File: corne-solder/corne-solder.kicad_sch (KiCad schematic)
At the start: 47 parts, among them J1 Battery Connector, J2 nice!view, SW1 SW_Push, SW10 SW_Push, SW11 SW_Push, SW12 SW_Push, SW13 SW_Push, SW14 SW_Push, SW15 SW_Push, SW16 SW_Push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

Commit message: update
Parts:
- D1, D10, D11, D12, D13, D14, D15, D16, D17, D18, D19, D2, D20, D21, D3, D4, D5, D6, D7, D8, D9: footprint Project:D_SOD-123F-Reversible-Solder -> Project:Diode-Reversible
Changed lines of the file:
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@@
 			)
 		)
-		(property "Footprint" "Project:D_SOD-123F-Reversible-Solder"
+		(property "Footprint" "Project:Diode-Reversible"
 			(at 232.41 102.87 0)
 			(effects
@@
 			)
 		)
-		(property "Footprint" "Project:D_SOD-123F-Reversible-Solder"
+		(property "Footprint" "Project:Diode-Reversible"
 			(at 214.63 120.65 0)
 			(effects
@@
 			)
 		)
-		(property "Footprint" "Project:D_SOD-123F-Reversible-Solder"
+		(property "Footprint" "Project:Diode-Reversible"
 			(at 250.19 156.21 0)
 			(effects
@@
 			)
 		)
-		(property "Footprint" "Project:D_SOD-123F-Reversible-Solder"
+		(property "Footprint" "Project:Diode-Reversible"
 			(at 214.63 138.43 0)
 			(effects
@@
 			)
 		)
-		(property "Footprint" "Project:D_SOD-123F-Reversible-Solder"
+		(property "Footprint" "Project:Diode-Reversible"
 			(at 196.85 120.65 0)
 			(effects
@@
 			)
 		)
-		(property "Footprint" "Project:D_SOD-123F-Reversible-Solder"
+		(property "Footprint" "Project:Diode-Reversible"
 			(at 179.07 102.87 0)
 			(effects
@@
 			)
 		)
-		(property "Footprint" "Project:D_SOD-123F-Reversible-Solder"
+		(property "Footprint" "Project:Diode-Reversible"
 			(at 179.07 138.43 0)
 			(effects
@@
 			)
 		)
-		(property "Footprint" "Project:D_SOD-123F-Reversible-Solder"
+		(property "Footprint" "Project:Diode-Reversible"
 			(at 179.07 120.65 0)
 			(effects
@@
 			)
 		)
-		(property "Footprint" "Project:D_SOD-123F-Reversible-Solder"
+		(property "Footprint" "Project:Diode-Reversible"
 			(at 196.85 102.87 0)
 			(effects
@@
 			)
 		)
-		(property "Footprint" "Project:D_SOD-123F-Reversible-Solder"
+		(property "Footprint" "Project:Diode-Reversible"
 			(at 267.97 102.87 0)
 			(effects
@@
 			)
 		)
-		(property "Footprint" "Project:D_SOD-123F-Reversible-Solder"
+		(property "Footprint" "Project:Diode-Reversible"
 			(at 267.97 138.43 0)
 			(effects
@@
 			)
 		)
-		(property "Footprint" "Project:D_SOD-123F-Reversible-Solder"
+		(property "Footprint" "Project:Diode-Reversible"
 			(at 214.63 102.87 0)
 			(effects
@@
 			)
 		)
-		(property "Footprint" "Project:D_SOD-123F-Reversible-Solder"
+		(property "Footprint" "Project:Diode-Reversible"
 			(at 267.97 156.21 0)
 			(effects
@@
 			)
 		)
-		(property "Footprint" "Project:D_SOD-123F-Reversible-Solder"
+		(property "Footprint" "Project:Diode-Reversible"
 			(at 232.41 120.65 0)
 			(effects
@@
 			)
 		)
-		(property "Footprint" "Project:D_SOD-123F-Reversible-Solder"
+		(property "Footprint" "Project:Diode-Reversible"
 			(at 250.19 138.43 0)
 			(effects
@@
 			)
 		)
-		(property "Footprint" "Project:D_SOD-123F-Reversible-Solder"
+		(property "Footprint" "Project:Diode-Reversible"
 			(at 232.41 156.21 0)
 			(effects
@@
 			)
 		)
-		(property "Footprint" "Project:D_SOD-123F-Reversible-Solder"
+		(property "Footprint" "Project:Diode-Reversible"
 			(at 267.97 120.65 0)
 			(effects
@@
 			)
 		)
-		(property "Footprint" "Project:D_SOD-123F-Reversible-Solder"
+		(property "Footprint" "Project:Diode-Reversible"
 			(at 196.85 138.43 0)
 			(effects
@@
 			)
 		)
-		(property "Footprint" "Project:D_SOD-123F-Reversible-Solder"
+		(property "Footprint" "Project:Diode-Reversible"
 			(at 250.19 102.87 0)
 			(effects
@@
 			)
 		)
-		(property "Footprint" "Project:D_SOD-123F-Reversible-Solder"
+		(property "Footprint" "Project:Diode-Reversible"
 			(at 250.19 120.65 0)
 			(effects
@@
 			)
 		)
-		(property "Footprint" "Project:D_SOD-123F-Reversible-Solder"
+		(property "Footprint" "Project:Diode-Reversible"
 			(at 232.41 138.43 0)
 			(effects

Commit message: wiring
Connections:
- net GND: now also J1.1 (Pin_1); no longer J1.2 (Pin_2)
- net at PSW1.2 (B): now also J1.2 (Pin_2); no longer J1.1 (Pin_1)
- no-connect marks 3 -> 6
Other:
- moved on the sheet: J1
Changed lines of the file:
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@@
 	)
 	(no_connect
+		(at 45.72 74.93)
+	)
+	(no_connect
 		(at 45.72 52.07)
 	)
 	(no_connect
+		(at 71.12 77.47)
+	)
+	(no_connect
 		(at 45.72 49.53)
 	)
@@
 		(at 48.26 101.6)
 	)
+	(no_connect
+		(at 71.12 74.93)
+	)
 	(wire
 		(pts
@@
 	(wire
 		(pts
+			(xy 66.04 104.14) (xy 58.42 104.14)
+		)
+		(stroke
+			(width 0)
+			(type default)
+		)
+	)
+	(wire
+		(pts
 			(xy 257.81 90.17) (xy 257.81 99.06)
 		)
@@
 	(wire
 		(pts
-			(xy 58.42 104.14) (xy 66.04 104.14)
-		)
-		(stroke
-			(width 0)
-			(type default)
-		)
-	)
-	(wire
-		(pts
 			(xy 168.91 116.84) (xy 168.91 134.62)
 		)
@@
 	(symbol
 		(lib_id "Connector_Generic:Conn_01x02")
-		(at 71.12 104.14 0)
+		(at 71.12 101.6 0)
 		(unit 1)
 		(exclude_from_sim no)
@@
 		(fields_autoplaced yes)
 		(property "Reference" "J1"
-			(at 73.66 104.1399 0)
+			(at 73.66 101.5999 0)
 			(effects
 				(font
@@
 		)
 		(property "Value" "Battery Connector"
-			(at 73.66 106.6799 0)
+			(at 73.66 104.1399 0)
 			(effects
 				(font
@@
 		)
 		(property "Footprint" "Connector_JST:JST_PH_S2B-PH-K_1x02_P2.00mm_Horizontal"
-			(at 71.12 104.14 0)
+			(at 71.12 101.6 0)
 			(effects
 				(font
@@
 		)
 		(property "Datasheet" "~"
-			(at 71.12 104.14 0)
+			(at 71.12 101.6 0)
 			(effects
 				(font
@@
 		)
 		(property "Description" "Generic connector, single row, 01x02, script generated (kicad-library-utils/schlib/autogen/connector/)"
-			(at 71.12 104.14 0)
+			(at 71.12 101.6 0)
 			(effects
 				(font
@@
 	)
 	(symbol
-		(lib_id "power:GND")
-		(at 66.04 106.68 270)
-		(unit 1)
-		(exclude_from_sim no)
-		(in_bom yes)
-		(on_board yes)
-		(dnp no)
-		(fields_autoplaced yes)
-		(property "Reference" "#PWR02"
-			(at 59.69 106.68 0)
-			(effects
-				(font
-					(size 1.27 1.27)
-				)
-				(hide yes)
-			)
-		)
-		(property "Value" "GND"
-			(at 62.23 106.6799 90)
-			(effects
-				(font
-					(size 1.27 1.27)
-				)
-				(justify right)
-			)
-		)
-		(property "Footprint" ""
-			(at 66.04 106.68 0)
-			(effects
-				(font
-					(size 1.27 1.27)
-				)
-				(hide yes)
-			)
-		)
-		(property "Datasheet" ""
-			(at 66.04 106.68 0)
-			(effects
-				(font
-					(size 1.27 1.27)
-				)
-				(hide yes)
-			)
-		)
-		(property "Description" "Power symbol creates a global label with name \"GND\" , ground"
-			(at 66.04 106.68 0)
-			(effects
-				(font
-					(size 1.27 1.27)
-				)
-				(hide yes)
-			)
-		)
-		(pin "1"
-		)
-		(instances
-			(project "corne-hotswap"
-				(path "/a84e1b1a-6de0-41da-b249-d0af4d1e6311"
-					(reference "#PWR02")
-					(unit 1)
-				)
-			)
-		)
-	)
-	(symbol
 		(lib_id "Device:D")
 		(at 196.85 120.65 90)
@@
 					(unit 1)
 				)
+			)
+		)
+	)
+	(symbol
+		(lib_id "power:GND")
+		(at 66.04 101.6 270)
+		(unit 1)
+		(exclude_from_sim no)
+		(in_bom yes)
+		(on_board yes)
+		(dnp no)
+		(fields_autoplaced yes)
+		(property "Reference" "#PWR02"
+			(at 59.69 101.6 0)
+			(effects
+				(font
+					(size 1.27 1.27)
+				)
+				(hide yes)
+			)
+		)
+		(property "Value" "GND"
+			(at 62.23 101.5999 90)
+			(effects
+				(font
+					(size 1.27 1.27)
+				)
+				(justify right)
+			)
+		)
+		(property "Footprint" ""
+			(at 66.04 101.6 0)
+			(effects
+				(font
+					(size 1.27 1.27)
+				)
+				(hide yes)
+			)
+		)
+		(property "Datasheet" ""
+			(at 66.04 101.6 0)
+			(effects
+				(font
+					(size 1.27 1.27)
+				)
+				(hide yes)
+			)
+		)
+		(property "Description" "Power symbol creates a global label with name \"GND\" , ground"
+			(at 66.04 101.6 0)
+			(effects
+				(font
+					(size 1.27 1.27)
+				)
+				(hide yes)
+			)
+		)
+		(pin "1"
+		)
+		(instances
+			(project "corne-solder"
+				(path "/a84e1b1a-6de0-41da-b249-d0af4d1e6311"
+					(reference "#PWR02")
+					(unit 1)
+				)

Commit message: More jump pads
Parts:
- J1: footprint Connector_JST:JST_PH_S2B-PH-K_1x02_P2.00mm_Horizontal -> Project:JST_PH_S2B-PH-K_1x02_P2.00mm_Horizontal
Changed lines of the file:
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@@
 			)
 		)
-		(property "Footprint" "Connector_JST:JST_PH_S2B-PH-K_1x02_P2.00mm_Horizontal"
+		(property "Footprint" "Project:JST_PH_S2B-PH-K_1x02_P2.00mm_Horizontal"
 			(at 71.12 101.6 0)
 			(effects

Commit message: add bridge for wired
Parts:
- added J3: USB_C_Receptacle_PowerOnly_6P, Project:USB_C_Receptacle_GCT_USB4125-xx-x_6P_TopMnt_Horizontal, symbol Connector:USB_C_Receptacle_PowerOnly_6P
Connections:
- net GND: now also J3.A12 (GND), J3.B12 (GND), J3.S1 (SHIELD)
- net VCC: now also J3.A9 (VBUS), J3.B9 (VBUS)
- net RX: now reaches U1.2 (D2-RX)
- net RX: now also J3.A5 (CC1), J3.B5 (CC2)
- no-connect marks 6 -> 5
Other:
- moved on the sheet: J1, J2, PSW1, RSW1

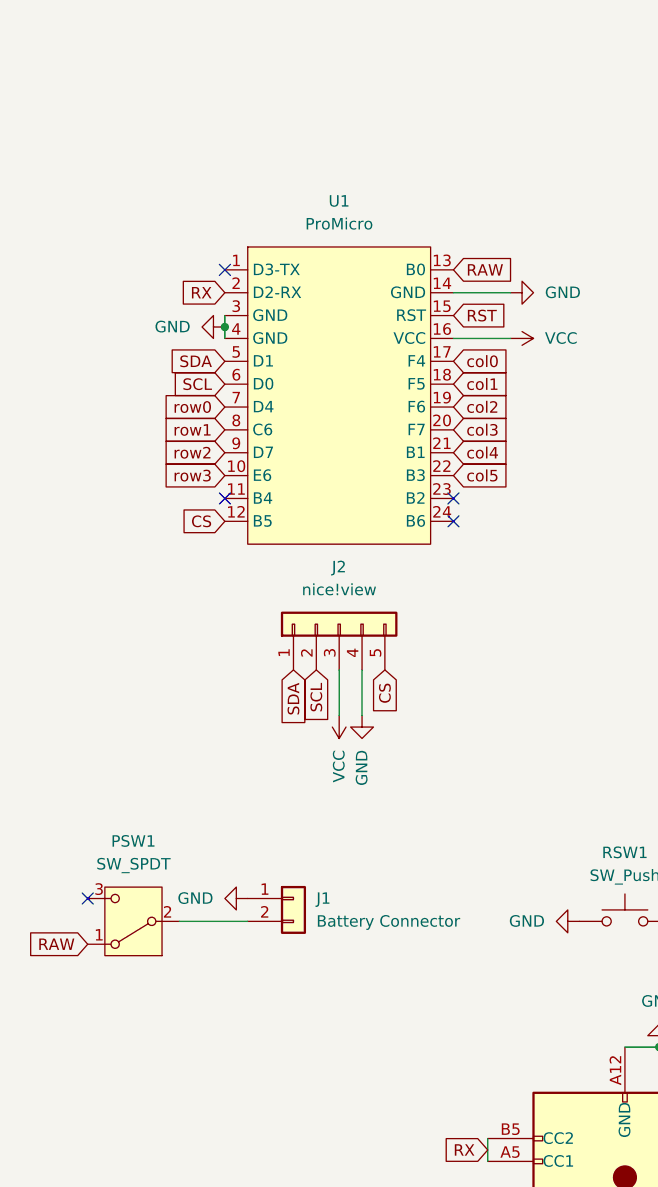
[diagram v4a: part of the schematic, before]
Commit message: add battery wire pads
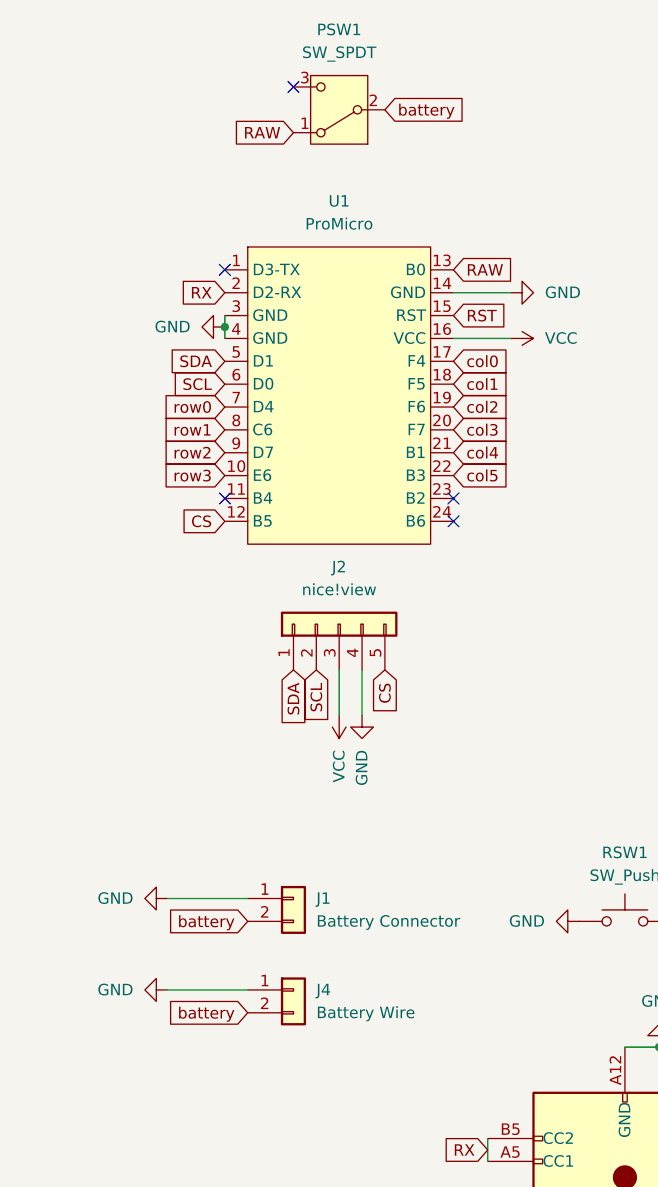
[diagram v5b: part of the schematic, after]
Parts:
- added J4: Battery Wire, Project:Battery Wire, symbol Connector_Generic:Conn_01x02
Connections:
- net GND: now also J4.1 (Pin_1)
- net battery: now reaches J1.2 (Pin_2), PSW1.2 (B)
- net battery: now also J4.2 (Pin_2)
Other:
- moved on the sheet: PSW1
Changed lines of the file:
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@@
 	)
 	(no_connect
-		(at 30.48 119.38)
+		(at 53.34 29.21)
 	)
 	(no_connect
@@
 	(wire
 		(pts
-			(xy 48.26 121.92) (xy 40.64 121.92)
-		)
-		(stroke
-			(width 0)
-			(type default)
-		)
-	)
-	(wire
-		(pts
 			(xy 257.81 90.17) (xy 257.81 99.06)
 		)
@@
 	(wire
 		(pts
+			(xy 39.37 119.38) (xy 48.26 119.38)
+		)
+		(stroke
+			(width 0)
+			(type default)
+		)
+	)
+	(wire
+		(pts
 			(xy 267.97 124.46) (xy 273.05 124.46)
 		)
@@
 	(wire
 		(pts
+			(xy 39.37 129.54) (xy 48.26 129.54)
+		)
+		(stroke
+			(width 0)
+			(type default)
+		)
+	)
+	(wire
+		(pts
 			(xy 179.07 124.46) (xy 196.85 124.46)
 		)
@@
 		)
 	)
+	(global_label "battery"
+		(shape input)
+		(at 63.5 31.75 0)
+		(fields_autoplaced yes)
+		(effects
+			(font
+				(size 1.27 1.27)
+			)
+			(justify left)
+		)
+		(property "Intersheetrefs" "${INTERSHEET_REFS}"
+			(at 73.077 31.75 0)
+			(effects
+				(font
+					(size 1.27 1.27)
+				)
+				(justify left)
+				(hide yes)
+			)
+		)
+	)
 	(global_label "col5"
 		(shape input)
@@
 	(global_label "RAW"
 		(shape input)
-		(at 30.48 124.46 180)
+		(at 53.34 34.29 180)
 		(fields_autoplaced yes)
 		(effects
@@
 		)
 		(property "Intersheetrefs" "${INTERSHEET_REFS}"
-			(at 23.6848 124.46 0)
+			(at 46.5448 34.29 0)
 			(effects
 				(font
@@
 		)
 	)
+	(global_label "battery"
+		(shape input)
+		(at 48.26 132.08 180)
+		(fields_autoplaced yes)
+		(effects
+			(font
+				(size 1.27 1.27)
+			)
+			(justify right)
+		)
+		(property "Intersheetrefs" "${INTERSHEET_REFS}"
+			(at 38.683 132.08 0)
+			(effects
+				(font
+					(size 1.27 1.27)
+				)
+				(justify right)
+				(hide yes)
+			)
+		)
+	)
 	(global_label "col5"
 		(shape input)
@@
 		)
 	)
+	(global_label "battery"
+		(shape input)
+		(at 48.26 121.92 180)
+		(fields_autoplaced yes)
+		(effects
+			(font
+				(size 1.27 1.27)
+			)
+			(justify right)
+		)
+		(property "Intersheetrefs" "${INTERSHEET_REFS}"
+			(at 38.683 121.92 0)
+			(effects
+				(font
+					(size 1.27 1.27)
+				)
+				(justify right)
+				(hide yes)
+			)
+		)
+	)
 	(symbol
 		(lib_id "power:VCC")
@@
 	)
 	(symbol
+		(lib_id "Connector_Generic:Conn_01x02")
+		(at 53.34 129.54 0)
+		(unit 1)
+		(exclude_from_sim no)
+		(in_bom yes)
+		(on_board yes)
+		(dnp no)
+		(fields_autoplaced yes)
+		(property "Reference" "J4"
+			(at 55.88 129.5399 0)
+			(effects
+				(font
+					(size 1.27 1.27)
+				)
+				(justify left)
+			)
+		)
+		(property "Value" "Battery Wire"
+			(at 55.88 132.0799 0)
+			(effects
+				(font
+					(size 1.27 1.27)
+				)
+				(justify left)
+			)
+		)
+		(property "Footprint" "Project:Battery Wire"
+			(at 53.34 129.54 0)
+			(effects
+				(font
+					(size 1.27 1.27)
+				)
+				(hide yes)
+			)
+		)
+		(property "Datasheet" "~"
+			(at 53.34 129.54 0)
+			(effects
+				(font
+					(size 1.27 1.27)
+				)
+				(hide yes)
+			)
+		)
+		(property "Description" "Generic connector, single row, 01x02, script generated (kicad-library-utils/schlib/autogen/connector/)"
+			(at 53.34 129.54 0)
+			(effects
+				(font
+					(size 1.27 1.27)
+				)
+				(hide yes)
+			)
+		)
+		(pin "2"
+		)
+		(pin "1"
+		)
+		(instances
+			(project "corne-solder"
+				(path "/a84e1b1a-6de0-41da-b249-d0af4d1e6311"
+					(reference "J4")
+					(unit 1)
+				)
+			)
+		)
+	)
+	(symbol
+		(lib_id "power:GND")
+		(at 39.37 129.54 270)
+		(unit 1)
+		(exclude_from_sim no)
+		(in_bom yes)
+		(on_board yes)
+		(dnp no)
+		(fields_autoplaced yes)
+		(property "Reference" "#PWR010"
+			(at 33.02 129.54 0)
+			(effects
+				(font
+					(size 1.27 1.27)
+				)
+				(hide yes)
+			)
+		)
+		(property "Value" "GND"
+			(at 35.56 129.5399 90)
+			(effects
+				(font
+					(size 1.27 1.27)
+				)
+				(justify right)
+			)
+		)
+		(property "Footprint" ""
+			(at 39.37 129.54 0)
+			(effects
+				(font
+					(size 1.27 1.27)
+				)
+				(hide yes)
+			)
+		)
+		(property "Datasheet" ""
+			(at 39.37 129.54 0)
+			(effects
+				(font
+					(size 1.27 1.27)
+				)
+				(hide yes)
+			)
+		)
+		(property "Description" "Power symbol creates a global label with name \"GND\" , ground"
+			(at 39.37 129.54 0)
+			(effects
+				(font
+					(size 1.27 1.27)
+				)
+				(hide yes)
+			)
+		)
+		(pin "1"
+		)
+		(instances
+			(project "corne-solder"
+				(path "/a84e1b1a-6de0-41da-b249-d0af4d1e6311"
+					(reference "#PWR010")
+					(unit 1)
+				)
+			)
+		)
+	)
+	(symbol
 		(lib_id "power:GND")
 		(at 60.96 99.06 0)
@@
 	(symbol
 		(lib_id "power:GND")
-		(at 48.26 119.38 270)
+		(at 39.37 119.38 270)
 		(unit 1)
 		(exclude_from_sim no)
@@
 		(fields_autoplaced yes)
 		(property "Reference" "#PWR02"
-			(at 41.91 119.38 0)
+			(at 33.02 119.38 0)
 			(effects
 				(font
@@
 		)
 		(property "Value" "GND"
-			(at 44.45 119.3799 90)
+			(at 35.56 119.3799 90)
 			(effects
 				(font
@@
 		)
 		(property "Footprint" ""
-			(at 48.26 119.38 0)
+			(at 39.37 119.38 0)
 			(effects
 				(font
@@
 		)
 		(property "Datasheet" ""
-			(at 48.26 119.38 0)
+			(at 39.37 119.38 0)
 			(effects
 				(font
@@
 		)
 		(property "Description" "Power symbol creates a global label with name \"GND\" , ground"
-			(at 48.26 119.38 0)
+			(at 39.37 119.38 0)
 			(effects
 				(font
@@
 	(symbol
 		(lib_id "Switch:SW_SPDT")
-		(at 35.56 121.92 180)
+		(at 58.42 31.75 180)
 		(unit 1)
 		(exclude_from_sim no)
@@
 		(fields_autoplaced yes)
 		(property "Reference" "PSW1"
-			(at 35.56 113.03 0)
+			(at 58.42 22.86 0)
 			(effects
 				(font
@@
 		)
 		(property "Value" "SW_SPDT"
-			(at 35.56 115.57 0)
+			(at 58.42 25.4 0)
 			(effects
 				(font
@@
 		)
 		(property "Footprint" "Project:SW_SPDT_PCM12"
-			(at 35.56 121.92 0)
+			(at 58.42 31.75 0)
 			(effects
 				(font
@@
 		)
 		(property "Datasheet" "~"
-			(at 35.56 114.3 0)
+			(at 58.42 24.13 0)
 			(effects
 				(font
@@
 		)
 		(property "Description" "Switch, single pole double throw"
-			(at 35.56 121.92 0)
+			(at 58.42 31.75 0)
 			(effects
 				(font

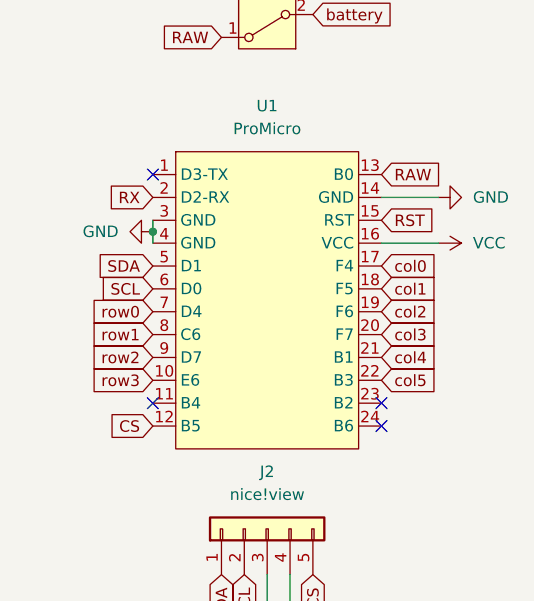
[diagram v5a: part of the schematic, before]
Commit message: move cs to default pinout
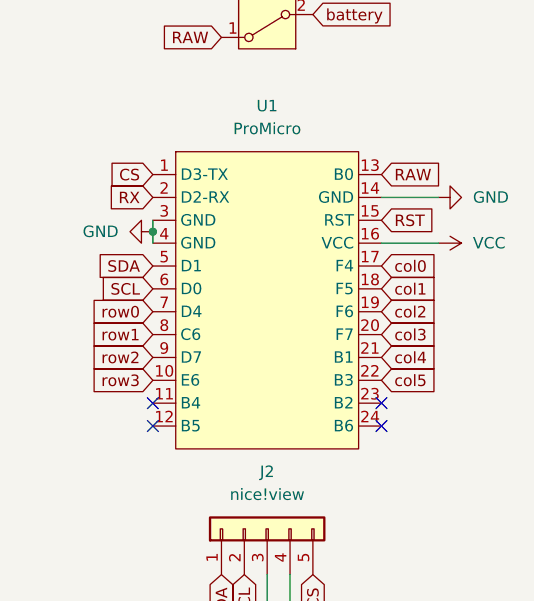
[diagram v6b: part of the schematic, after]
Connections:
- net CS: now also U1.1 (D3-TX); no longer U1.12 (B5)
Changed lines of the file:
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@@
 	)
 	(no_connect
-		(at 45.72 49.53)
+		(at 45.72 77.47)
 	)
 	(no_connect
@@
 		)
 	)
+	(global_label "row0"
+		(shape input)
+		(at 45.72 64.77 180)
+		(fields_autoplaced yes)
+		(effects
+			(font
+				(size 1.27 1.27)
+			)
+			(justify right)
+		)
+		(property "Intersheetrefs" "${INTERSHEET_REFS}"
+			(at 38.2596 64.77 0)
+			(effects
+				(font
+					(size 1.27 1.27)
+				)
+				(justify right)
+				(hide yes)
+			)
+		)
+	)
+	(global_label "RST"
+		(shape input)
+		(at 71.12 54.61 0)
+		(fields_autoplaced yes)
+		(effects
+			(font
+				(size 1.27 1.27)
+			)
+			(justify left)
+		)
+		(property "Intersheetrefs" "${INTERSHEET_REFS}"
+			(at 77.5523 54.61 0)
+			(effects
+				(font
+					(size 1.27 1.27)
+				)
+				(justify left)
+				(hide yes)
+			)
+		)
+	)
 	(global_label "CS"
 		(shape input)
-		(at 45.72 77.47 180)
-		(fields_autoplaced yes)
-		(effects
-			(font
-				(size 1.27 1.27)
-			)
-			(justify right)
-		)
-		(property "Intersheetrefs" "${INTERSHEET_REFS}"
-			(at 40.2553 77.47 0)
-			(effects
-				(font
-					(size 1.27 1.27)
-				)
-				(justify right)
-				(hide yes)
-			)
-		)
-	)
-	(global_label "row0"
-		(shape input)
-		(at 45.72 64.77 180)
-		(fields_autoplaced yes)
-		(effects
-			(font
-				(size 1.27 1.27)
-			)
-			(justify right)
-		)
-		(property "Intersheetrefs" "${INTERSHEET_REFS}"
-			(at 38.2596 64.77 0)
-			(effects
-				(font
-					(size 1.27 1.27)
-				)
-				(justify right)
-				(hide yes)
-			)
-		)
-	)
-	(global_label "RST"
-		(shape input)
-		(at 71.12 54.61 0)
-		(fields_autoplaced yes)
-		(effects
-			(font
-				(size 1.27 1.27)
-			)
-			(justify left)
-		)
-		(property "Intersheetrefs" "${INTERSHEET_REFS}"
-			(at 77.5523 54.61 0)
-			(effects
-				(font
-					(size 1.27 1.27)
-				)
-				(justify left)
-				(hide yes)
-			)
+		(at 45.72 49.53 180)
+		(fields_autoplaced yes)
+		(effects
+			(font
+				(size 1.27 1.27)
+			)
+			(justify right)
+		)
+		(property "Intersheetrefs" "${INTERSHEET_REFS}"
+			(at 40.2553 49.53 0)
+			(effects
+				(font
+					(size 1.27 1.27)
+				)
+				(justify right)
+				(hide yes)
+			)
